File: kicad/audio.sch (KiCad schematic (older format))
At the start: 29 parts, among them J10 PC_AUDIO_EXTRA, J11 Jack header, J12 Jack header, J13 L/R channel choice, J14 Jack header, J15 CITA/OMTP choice, J16 TRRS/TRS+TS choice, J18 Xcvr grounding jumpers, J19 XCVR_Audio, J8 PC_AUDIO_IO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

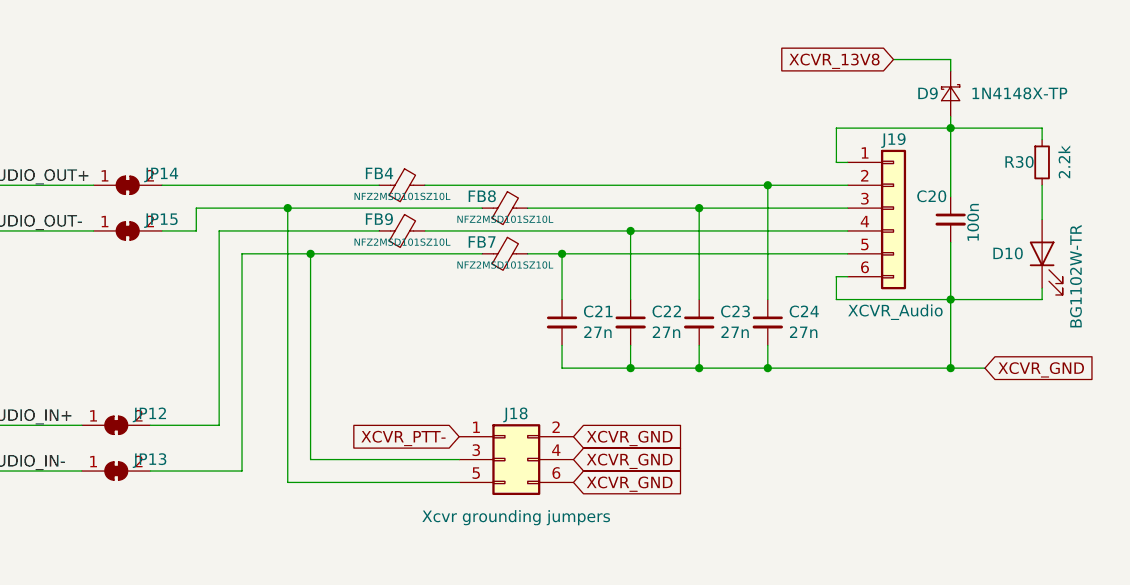
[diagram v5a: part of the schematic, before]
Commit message: Ferrite beads, hacking pads, audio fix
* Chose ferrite beads for IC Vcc (BLM31KN102SH1L)
* Change hacking pad thickness to 0.8mm
* Fixed potential oscillator when grounding audio- lines
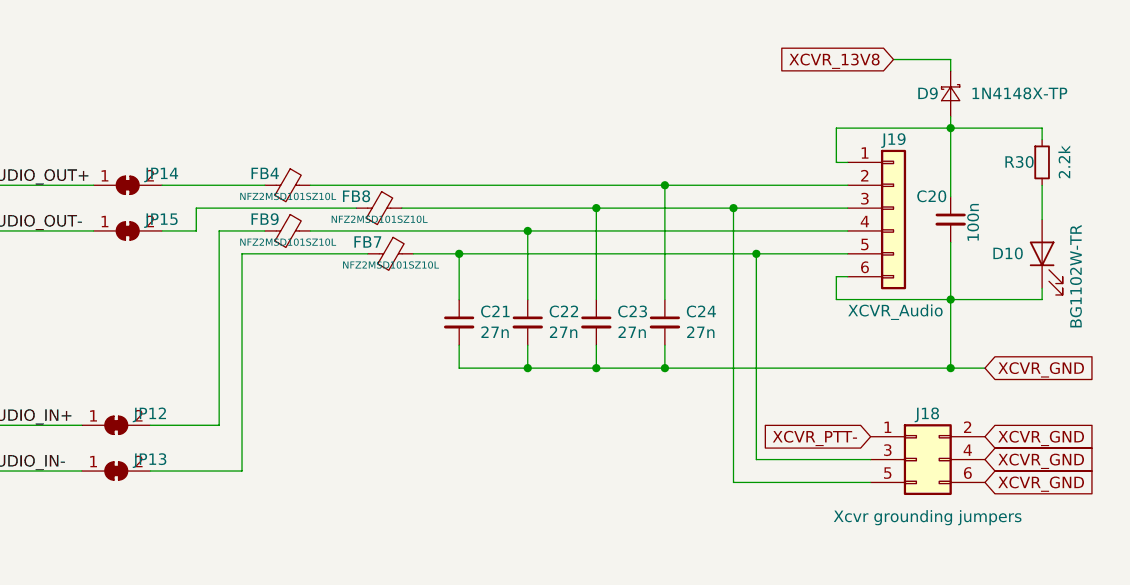
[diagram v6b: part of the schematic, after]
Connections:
- net at C23.1, FB8.1, J19.3 (Pin_3): now also J18.5 (Pin_5)
- net at C21.1, FB7.1, J19.5 (Pin_5): now also J18.3 (Pin_3)
- net at FB8.2, JP15.2 (B): no longer J18.5 (Pin_5)
- net at FB7.2, JP13.2 (B): no longer J18.3 (Pin_3)
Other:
- moved on the sheet: C21, C22, C23, C24, FB4, FB7, FB8, FB9, J18
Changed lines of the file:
@@
 Text GLabel 2450 4200 0    39   Input ~ 0
 PC_AUDIO_GND
-Text GLabel 8350 4550 0    50   Input ~ 0
+Text GLabel 10150 4550 0    50   Input ~ 0
 XCVR_PTT-
 Text Notes 5550 2800 1    50   ~ 0
@@
 Wire Wire Line
 	7400 4700 7400 3750
-Text GLabel 8850 4750 2    50   Input ~ 0
+Text GLabel 10650 4750 2    50   Input ~ 0
 XCVR_GND
-Text GLabel 8850 4650 2    50   Input ~ 0
+Text GLabel 10650 4650 2    50   Input ~ 0
 XCVR_GND
-Text GLabel 8850 4550 2    50   Input ~ 0
+Text GLabel 10650 4550 2    50   Input ~ 0
 XCVR_GND
 Wire Notes Line
@@
 L Connector_Generic:Conn_02x03_Odd_Even J18
 U 1 1 5FBEAB0B
-P 8550 4650
-F 0 "J18" H 8600 4850 50  0000 C CNN
-F 1 "Xcvr grounding jumpers" H 8600 4400 50  0000 C CNN
-F 2 "Connector_PinHeader_2.54mm:PinHeader_2x03_P2.54mm_Vertical" H 8550 4650 50  0001 C CNN
-F 3 "~" H 8550 4650 50  0001 C CNN
-	1    8550 4650
+P 10350 4650
+F 0 "J18" H 10400 4850 50  0000 C CNN
+F 1 "Xcvr grounding jumpers" H 10400 4400 50  0000 C CNN
+F 2 "Connector_PinHeader_2.54mm:PinHeader_2x03_P2.54mm_Vertical" H 10350 4650 50  0001 C CNN
+F 3 "~" H 10350 4650 50  0001 C CNN
+	1    10350 4650
 	1    0    0    -1
 $EndComp
@@
 Text Label 6050 3450 0    50   ~ 0
 XCVR_AUDIO_OUT+
-Wire Wire Line
-	7700 4650 8350 4650
-Wire Wire Line
-	7600 4750 8350 4750
 $Comp
 L Device:C_Small C24
 U 1 1 5FA2C807
-P 9700 4050
-F 0 "C24" H 9792 4096 50  0000 L CNN
-F 1 "27n" H 9792 4005 50  0000 L CNN
-F 2 "Capacitor_SMD:C_1206_3216Metric_Pad1.42x1.75mm_HandSolder" H 9700 4050 50  0001 C CNN
-F 3 "~" H 9700 4050 50  0001 C CNN
-	1    9700 4050
+P 9250 4050
+F 0 "C24" H 9342 4096 50  0000 L CNN
+F 1 "27n" H 9342 4005 50  0000 L CNN
+F 2 "Capacitor_SMD:C_1206_3216Metric_Pad1.42x1.75mm_HandSolder" H 9250 4050 50  0001 C CNN
+F 3 "~" H 9250 4050 50  0001 C CNN
+	1    9250 4050
 	1    0    0    -1
 $EndComp
@@
 L Device:C_Small C23
 U 1 1 5FA2ADBD
-P 9400 4050
-F 0 "C23" H 9492 4096 50  0000 L CNN
-F 1 "27n" H 9492 4005 50  0000 L CNN
-F 2 "Capacitor_SMD:C_1206_3216Metric_Pad1.42x1.75mm_HandSolder" H 9400 4050 50  0001 C CNN
-F 3 "~" H 9400 4050 50  0001 C CNN
-	1    9400 4050
+P 8950 4050
+F 0 "C23" H 9042 4096 50  0000 L CNN
+F 1 "27n" H 9042 4005 50  0000 L CNN
+F 2 "Capacitor_SMD:C_1206_3216Metric_Pad1.42x1.75mm_HandSolder" H 8950 4050 50  0001 C CNN
+F 3 "~" H 8950 4050 50  0001 C CNN
+	1    8950 4050
 	1    0    0    -1
 $EndComp
@@
 	10500 3950 10500 4250
 Wire Wire Line
-	10500 4250 9700 4250
-Wire Wire Line
-	9700 4250 9700 4150
-Connection ~ 10500 4250
-Wire Wire Line
-	9700 4250 9400 4250
-Wire Wire Line
-	9400 4250 9400 4150
-Connection ~ 9700 4250
+	9250 4250 9250 4150
+Wire Wire Line
+	9250 4250 8950 4250
+Wire Wire Line
+	8950 4250 8950 4150
+Connection ~ 9250 4250
 Wire Wire Line
 	1950 3450 5100 3450
@@
 L Device:C_Small C22
 U 1 1 5FA9E707
-P 9100 4050
-F 0 "C22" H 9192 4096 50  0000 L CNN
-F 1 "27n" H 9192 4005 50  0000 L CNN
-F 2 "Capacitor_SMD:C_1206_3216Metric_Pad1.42x1.75mm_HandSolder" H 9100 4050 50  0001 C CNN
-F 3 "~" H 9100 4050 50  0001 C CNN
-	1    9100 4050
+P 8650 4050
+F 0 "C22" H 8742 4096 50  0000 L CNN
+F 1 "27n" H 8742 4005 50  0000 L CNN
+F 2 "Capacitor_SMD:C_1206_3216Metric_Pad1.42x1.75mm_HandSolder" H 8650 4050 50  0001 C CNN
+F 3 "~" H 8650 4050 50  0001 C CNN
+	1    8650 4050
 	1    0    0    -1
 $EndComp
@@
 L Device:C_Small C21
 U 1 1 5FA9ECE0
-P 8800 4050
-F 0 "C21" H 8892 4096 50  0000 L CNN
-F 1 "27n" H 8892 4005 50  0000 L CNN
-F 2 "Capacitor_SMD:C_1206_3216Metric_Pad1.42x1.75mm_HandSolder" H 8800 4050 50  0001 C CNN
-F 3 "~" H 8800 4050 50  0001 C CNN
-	1    8800 4050
+P 8350 4050
+F 0 "C21" H 8442 4096 50  0000 L CNN
+F 1 "27n" H 8442 4005 50  0000 L CNN
+F 2 "Capacitor_SMD:C_1206_3216Metric_Pad1.42x1.75mm_HandSolder" H 8350 4050 50  0001 C CNN
+F 3 "~" H 8350 4050 50  0001 C CNN
+	1    8350 4050
 	1    0    0    -1
 $EndComp
@@
 L Device:Ferrite_Bead_Small FB4
 U 1 1 5FA9F658
-P 8100 3450
-F 0 "FB4" V 8050 3350 50  0000 C CNN
-F 1 "NFZ2MSD101SZ10L" V 8150 3450 31  0000 C CNN
-F 2 "custom:NFZ2MSD101SZ10L_0806_Handsolder" V 8030 3450 50  0001 C CNN
-F 3 "~" H 8100 3450 50  0001 C CNN
-	1    8100 3450
+P 7600 3450
+F 0 "FB4" V 7550 3350 50  0000 C CNN
+F 1 "NFZ2MSD101SZ10L" V 7650 3450 31  0000 C CNN
+F 2 "custom:NFZ2MSD101SZ10L_0806_Handsolder" V 7530 3450 50  0001 C CNN
+F 3 "~" H 7600 3450 50  0001 C CNN
+	1    7600 3450
 	0    1    1    0
 $EndComp
+$Comp
+L Device:Ferrite_Bead_Small FB9
+U 1 1 5FAA61AD
+P 7600 3650
+F 0 "FB9" V 7550 3550 50  0000 C CNN
+F 1 "NFZ2MSD101SZ10L" V 7650 3650 31  0000 C CNN
+F 2 "custom:NFZ2MSD101SZ10L_0806_Handsolder" V 7530 3650 50  0001 C CNN
+F 3 "~" H 7600 3650 50  0001 C CNN
+	1    7600 3650
+	0    1    1    0
+$EndComp
+$Comp
+L Device:Ferrite_Bead_Small FB7
+U 1 1 5FAAA821
+P 8050 3750
+F 0 "FB7" V 8000 3650 50  0000 C CNN
+F 1 "NFZ2MSD101SZ10L" V 8100 3750 31  0000 C CNN
+F 2 "custom:NFZ2MSD101SZ10L_0806_Handsolder" V 7980 3750 50  0001 C CNN
+F 3 "~" H 8050 3750 50  0001 C CNN
+	1    8050 3750
+	0    1    1    0
+$EndComp
+Wire Wire Line
+	8350 3750 8350 3950
+Wire Wire Line
+	8650 3650 8650 3950
+Wire Wire Line
+	8950 3950 8950 3550
+Wire Wire Line
+	9250 3950 9250 3450
+Wire Wire Line
+	8350 4150 8350 4250
+Wire Wire Line
+	8350 4250 8650 4250
+Connection ~ 8950 4250
+Wire Wire Line
+	8650 4150 8650 4250
+Connection ~ 8650 4250
+Wire Wire Line
+	8650 4250 8950 4250
+Wire Wire Line
+	7050 3650 7200 3650
+Wire Wire Line
+	7000 4700 7400 4700
+Wire Wire Line
+	7050 3450 7500 3450
+Wire Wire Line
+	7300 3650 7500 3650
+Wire Wire Line
+	9650 4650 9650 3750
+Wire Wire Line
+	9550 4750 9550 3550
+Wire Wire Line
+	7200 3550 7900 3550
 $Comp
 L Device:Ferrite_Bead_Small FB8
 U 1 1 5FAA5135
-P 8550 3550
-F 0 "FB8" V 8500 3450 50  0000 C CNN
-F 1 "NFZ2MSD101SZ10L" V 8600 3550 31  0000 C CNN
-F 2 "custom:NFZ2MSD101SZ10L_0806_Handsolder" V 8480 3550 50  0001 C CNN
-F 3 "~" H 8550 3550 50  0001 C CNN
-	1    8550 3550
+P 8000 3550
+F 0 "FB8" V 7950 3450 50  0000 C CNN
+F 1 "NFZ2MSD101SZ10L" V 8050 3550 31  0000 C CNN
+F 2 "custom:NFZ2MSD101SZ10L_0806_Handsolder" V 7930 3550 50  0001 C CNN
+F 3 "~" H 8000 3550 50  0001 C CNN
+	1    8000 3550
 	0    1    1    0
 $EndComp
-$Comp
-L Device:Ferrite_Bead_Small FB9
-U 1 1 5FAA61AD
-P 8100 3650
-F 0 "FB9" V 8050 3550 50  0000 C CNN
-F 1 "NFZ2MSD101SZ10L" V 8150 3650 31  0000 C CNN
-F 2 "custom:NFZ2MSD101SZ10L_0806_Handsolder" V 8030 3650 50  0001 C CNN
-F 3 "~" H 8100 3650 50  0001 C CNN
-	1    8100 3650
-	0    1    1    0
-$EndComp
-$Comp
-L Device:Ferrite_Bead_Small FB7
-U 1 1 5FAAA821
-P 8550 3750
-F 0 "FB7" V 8500 3650 50  0000 C CNN
-F 1 "NFZ2MSD101SZ10L" V 8600 3750 31  0000 C CNN
-F 2 "custom:NFZ2MSD101SZ10L_0806_Handsolder" V 8480 3750 50  0001 C CNN
-F 3 "~" H 8550 3750 50  0001 C CNN
-	1    8550 3750
-	0    1    1    0
-$EndComp
-Wire Wire Line
-	8800 3750 8800 3950
-Connection ~ 8800 3750
-Wire Wire Line
-	8800 3750 10050 3750
-Wire Wire Line
-	9100 3650 9100 3950
-Connection ~ 9100 3650
-Wire Wire Line
-	9100 3650 10050 3650
-Wire Wire Line
-	9400 3950 9400 3550
-Connection ~ 9400 3550
-Wire Wire Line
-	9400 3550 10050 3550
-Wire Wire Line
-	9700 3950 9700 3450
-Connection ~ 9700 3450
-Wire Wire Line
-	9700 3450 10050 3450
-Wire Wire Line
-	8800 4150 8800 4250
-Wire Wire Line
-	8800 4250 9100 4250
-Connection ~ 9400 4250
-Wire Wire Line
-	9100 4150 9100 4250
-Connection ~ 9100 4250
-Wire Wire Line
-	9100 4250 9400 4250
-Wire Wire Line
-	7050 3650 7200 3650
-Wire Wire Line
-	7000 4700 7400 4700
-Wire Wire Line
-	8650 3550 9400 3550
-Wire Wire Line
-	8650 3750 8800 3750
-Wire Wire Line
-	8200 3450 9700 3450
-Wire Wire Line
-	8200 3650 9100 3650
-Wire Wire Line
-	7050 3450 8000 3450
-Wire Wire Line
-	7200 3550 7600 3550
-Wire Wire Line
-	7300 3650 8000 3650
-Wire Wire Line
-	7400 3750 7700 3750
-Wire Wire Line
-	7700 4650 7700 3750
-Connection ~ 7700 3750
-Wire Wire Line
-	7700 3750 8450 3750
-Wire Wire Line
-	7600 4750 7600 3550
-Connection ~ 7600 3550
-Wire Wire Line
-	7600 3550 8450 3550
+Wire Wire Line
+	7700 3450 9250 3450
+Wire Wire Line
+	8100 3550 8950 3550
+Wire Wire Line
+	7700 3650 8650 3650
+Wire Wire Line
+	7400 3750 7950 3750
+Wire Wire Line
+	8150 3750 8350 3750
+Connection ~ 8350 3750
+Connection ~ 8650 3650
+Connection ~ 8950 3550
+Connection ~ 9250 3450
+Wire Wire Line
+	8350 3750 9650 3750
+Wire Wire Line
+	8650 3650 10050 3650
+Wire Wire Line
+	8950 3550 9550 3550
+Wire Wire Line
+	9250 3450 10050 3450
+Wire Wire Line
+	9250 4250 10500 4250
+Connection ~ 10500 4250
+Connection ~ 9550 3550
+Wire Wire Line
+	9550 3550 10050 3550
+Connection ~ 9650 3750
+Wire Wire Line
+	9650 3750 10050 3750
+Wire Wire Line
+	9650 4650 10150 4650
+Wire Wire Line
+	9550 4750 10150 4750
 $EndSCHEMATC

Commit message: Small fixes
* Moved via that was unreasonably close to another one
* Changed 13V8 diodes to SM5819PL-TP
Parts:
- D9: value 1N4148X-TP -> SM5819PL-TP; footprint Diode_SMD:D_SOD-523 -> Diode_SMD:D_SOD-123F
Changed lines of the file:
@@
 AR Path="/5F9E817D/5FC37881" Ref="D9"  Part="1"
 F 0 "D9" V 10500 2950 50  0000 C CNN
-F 1 "1N4148X-TP" V 10500 3350 50  0000 C CNN
-F 2 "Diode_SMD:D_SOD-523" V 10500 3050 50  0001 C CNN
+F 1 "SM5819PL-TP" V 10500 3350 50  0000 C CNN
+F 2 "Diode_SMD:D_SOD-123F" V 10500 3050 50  0001 C CNN
 F 3 "~" V 10500 3050 50  0001 C CNN
 	1    10500 3050
